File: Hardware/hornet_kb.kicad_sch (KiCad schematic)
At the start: 28 parts, among them J1 Conn_ST_STDC14, J10 USB_C_Receptacle_USB2.0, SW98 SW_Push, U1 nRF52840, Y1 32.768kHz, Y2 32MHz

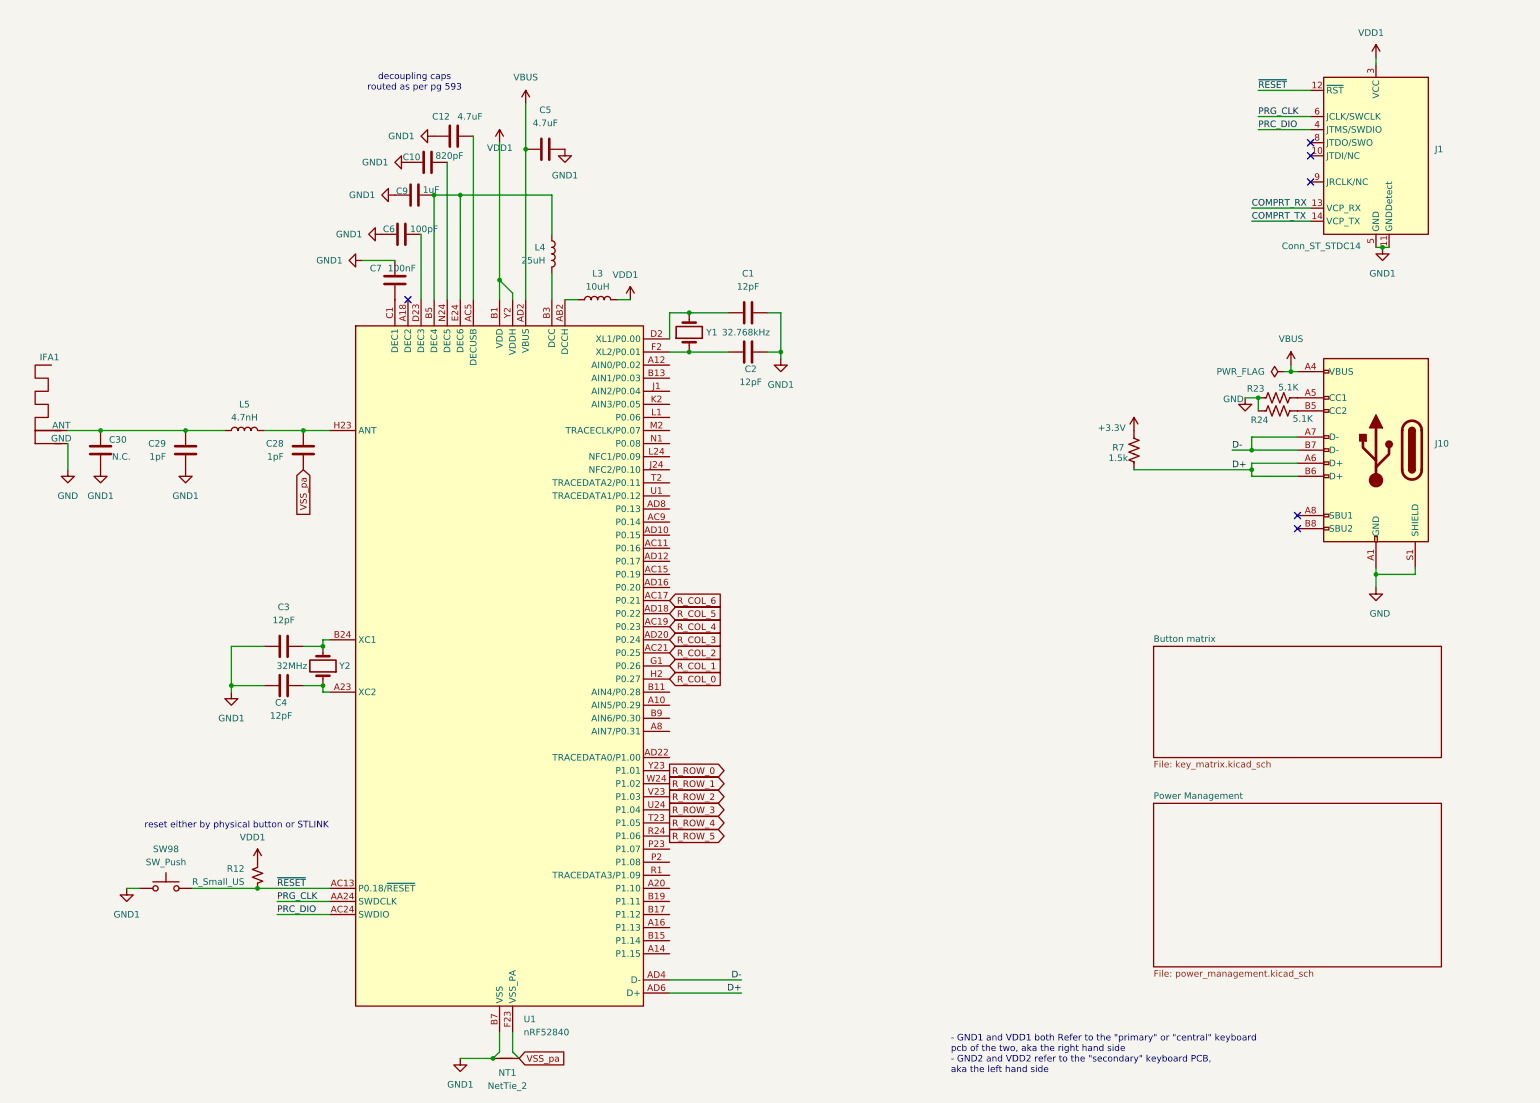
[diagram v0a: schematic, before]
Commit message: add datasheet to usb charger and fix erc
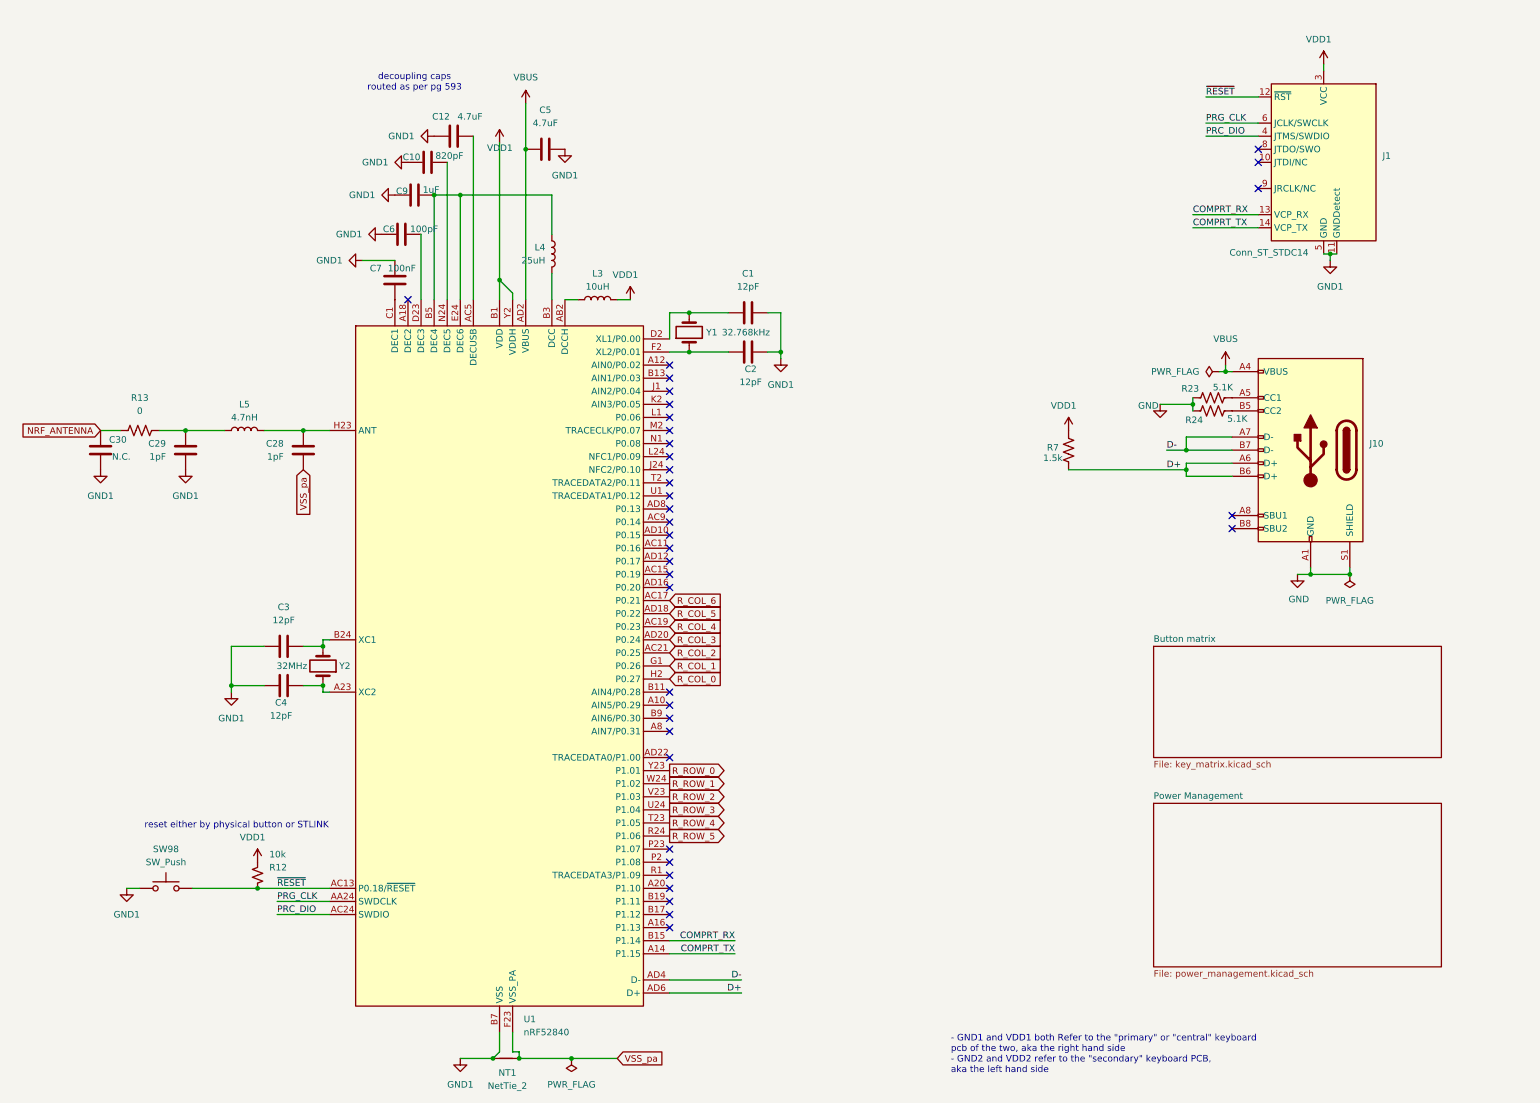
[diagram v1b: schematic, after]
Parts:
- removed IFA1: ~, symbol Device:IFA
- added R13: 0, symbol Device:R_US
- R12: value R_Small_US -> 10k
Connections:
- net +3.3V is gone; now on net VDD1: R7.1
- net COMPRT_RX: now also U1.B15 (P1.14)
- net COMPRT_TX: now also U1.A14 (P1.15)
- net at C29.1, L5.2: now also R13.2; no longer C30.1
- new net NRF_ANTENNA: C30.1, R13.1
- no-connect marks 6 -> 36
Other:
- moved on the sheet: J1, J10, R23, R24, R7

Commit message: Update footprints and switch symbol in schematic
Set proper SMD footprints for capacitors, resistors, inductors, crystals, and net ties in hornet_kb.kicad_sch. In power_management.kicad_sch, replace DIP switch symbol with DPDT switch, update related symbol properties, add new switch instance, and adjust wiring and annotation for improved clarity and functionality. Man i love summarize with copilot
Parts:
- C10, C6, C7, C9: footprint (none) -> Capacitor_SMD:C_0603_1608Metric
- C12, C5: footprint (none) -> Capacitor_SMD:C_0805_2012Metric
- C28, C29: footprint (none) -> Capacitor_SMD:C_0402_1005Metric
- L5: footprint (none) -> Inductor_SMD:L_0402_1005Metric
- NT1: footprint (none) -> NetTie:NetTie-2_SMD_Pad2.0mm
- R12: footprint (none) -> Resistor_SMD:R_0603_1608Metric
- R13: footprint (none) -> Resistor_SMD:R_0402_1005Metric
- Y1, Y2: footprint (none) -> Crystal:Crystal_SMD_3215-2Pin_3.2x1.5mm
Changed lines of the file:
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@@
 			)
 		)
-		(property "Footprint" ""
+		(property "Footprint" "Capacitor_SMD:C_0402_1005Metric"
 			(at 73.9648 102.87 0)
 			(effects
@@
 			)
 		)
-		(property "Footprint" ""
+		(property "Footprint" "Resistor_SMD:R_0603_1608Metric"
 			(at 66.04 181.61 0)
 			(effects
@@
 			)
 		)
-		(property "Footprint" ""
+		(property "Footprint" "Capacitor_SMD:C_0603_1608Metric"
 			(at 93.6752 62.23 0)
 			(effects
@@
 			)
 		)
-		(property "Footprint" ""
+		(property "Footprint" "Resistor_SMD:R_0402_1005Metric"
 			(at 43.434 94.234 90)
 			(effects
@@
 			)
 		)
-		(property "Footprint" ""
+		(property "Footprint" "NetTie:NetTie-2_SMD_Pad2.0mm"
 			(at 114.3 217.17 0)
 			(effects
@@
 			)
 		)
-		(property "Footprint" ""
+		(property "Footprint" "Inductor_SMD:L_0402_1005Metric"
 			(at 63.5 95.25 0)
 			(effects
@@
 			)
 		)
-		(property "Footprint" ""
+		(property "Footprint" "Capacitor_SMD:C_0603_1608Metric"
 			(at 90.17 56.1848 0)
 			(effects
@@
 			)
 		)
-		(property "Footprint" ""
+		(property "Footprint" "Crystal:Crystal_SMD_3215-2Pin_3.2x1.5mm"
 			(at 149.86 76.2 0)
 			(effects
@@
 			)
 		)
-		(property "Footprint" ""
+		(property "Footprint" "Capacitor_SMD:C_0805_2012Metric"
 			(at 118.11 39.6748 0)
 			(effects
@@
 			)
 		)
-		(property "Footprint" ""
+		(property "Footprint" "Capacitor_SMD:C_0805_2012Metric"
 			(at 100.33 37.1348 0)
 			(effects
@@
 			)
 		)
-		(property "Footprint" ""
+		(property "Footprint" "Capacitor_SMD:C_0603_1608Metric"
 			(at 92.71 48.5648 0)
 			(effects
@@
 			)
 		)
-		(property "Footprint" ""
+		(property "Footprint" "Crystal:Crystal_SMD_3215-2Pin_3.2x1.5mm"
 			(at 78.74 140.97 0)
 			(effects
@@
 			)
 		)
-		(property "Footprint" ""
+		(property "Footprint" "Capacitor_SMD:C_0402_1005Metric"
 			(at 51.1048 102.87 0)
 			(effects
@@
 			)
 		)
-		(property "Footprint" ""
+		(property "Footprint" "Capacitor_SMD:C_0603_1608Metric"
 			(at 102.87 44.1452 0)
 			(effects

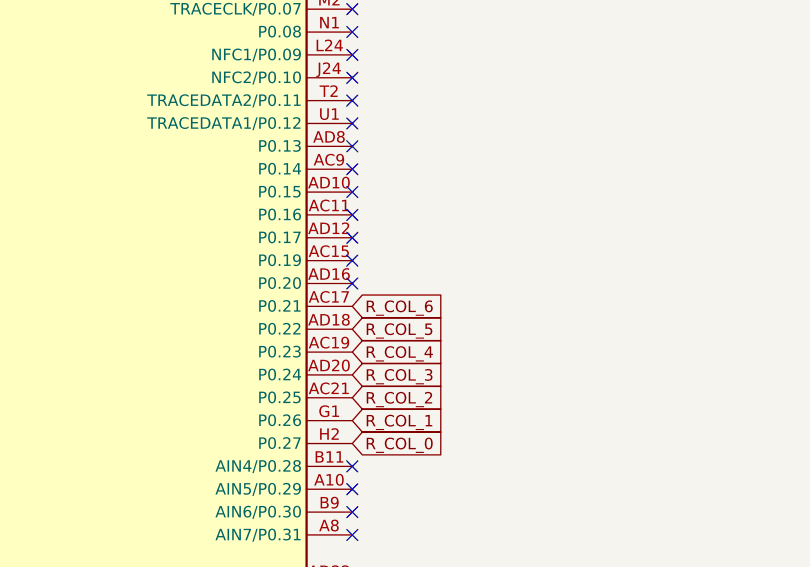
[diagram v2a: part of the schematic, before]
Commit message: Completed keymatrix layout
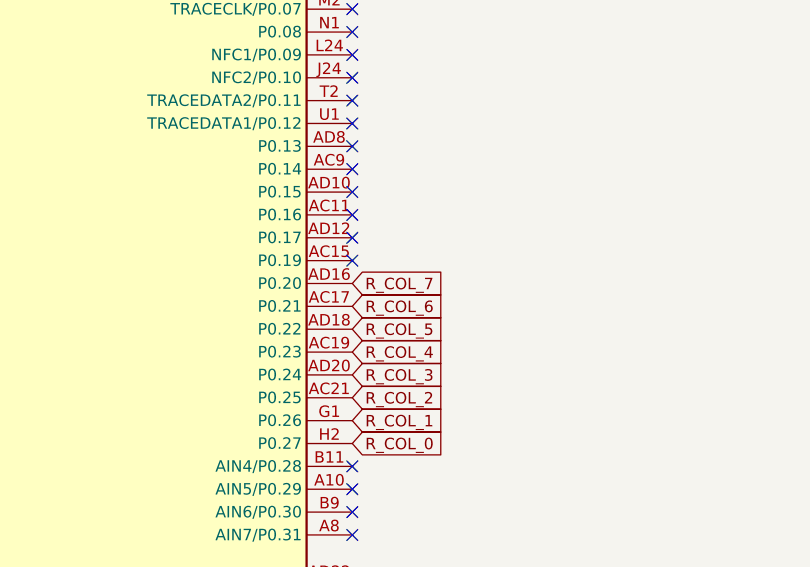
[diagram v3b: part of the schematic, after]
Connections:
- net R_COL_7: now reaches U1.AD16 (P0.20)
- no-connect marks 36 -> 35
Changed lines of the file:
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@@
 	)
 	(no_connect
-		(at 146.05 125.73)
-	)
-	(no_connect
 		(at 146.05 123.19)
 	)
@@
 			(effects
 				(font
+					(size 1.27 1.27)
+				)
+				(justify left)
+				(hide yes)
+			)
+		)
+	)
+	(global_label "R_COL_7"
+		(shape input)
+		(at 146.05 125.73 0)
+		(fields_autoplaced yes)
+		(effects
+			(font
+				(size 1.27 1.27)
+			)
+			(justify left)
+		)
+		(property "Intersheetrefs" "${INTERSHEET_REFS}"
+			(at 157.0785 125.73 0)
+			(effects
+				(font

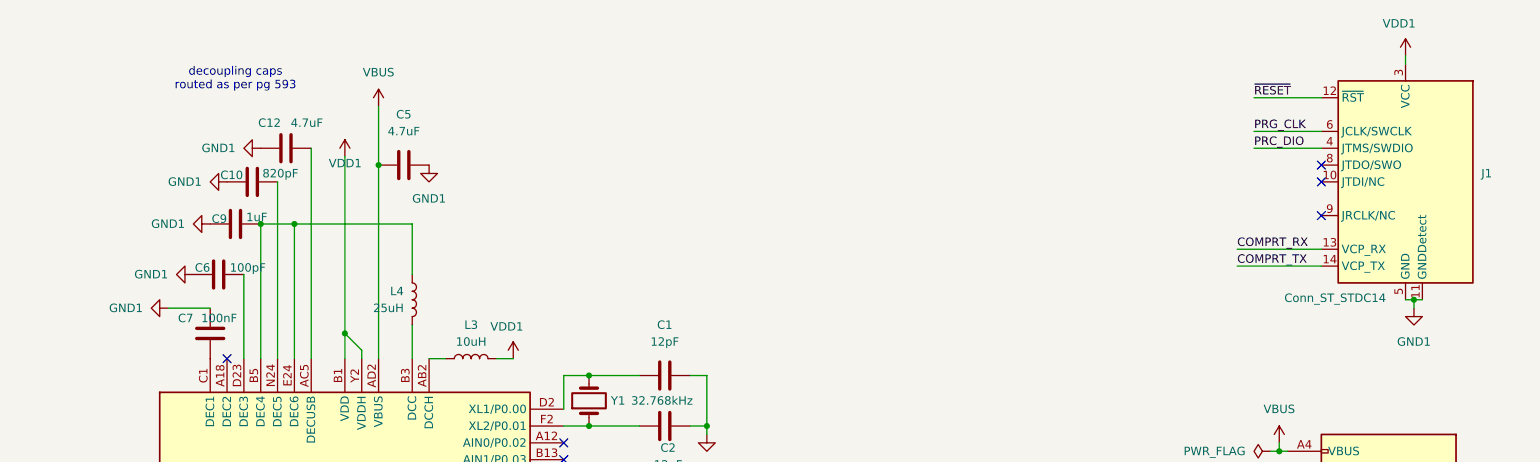
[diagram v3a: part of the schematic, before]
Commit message: Added LDO to battery and added placement for the charging modules
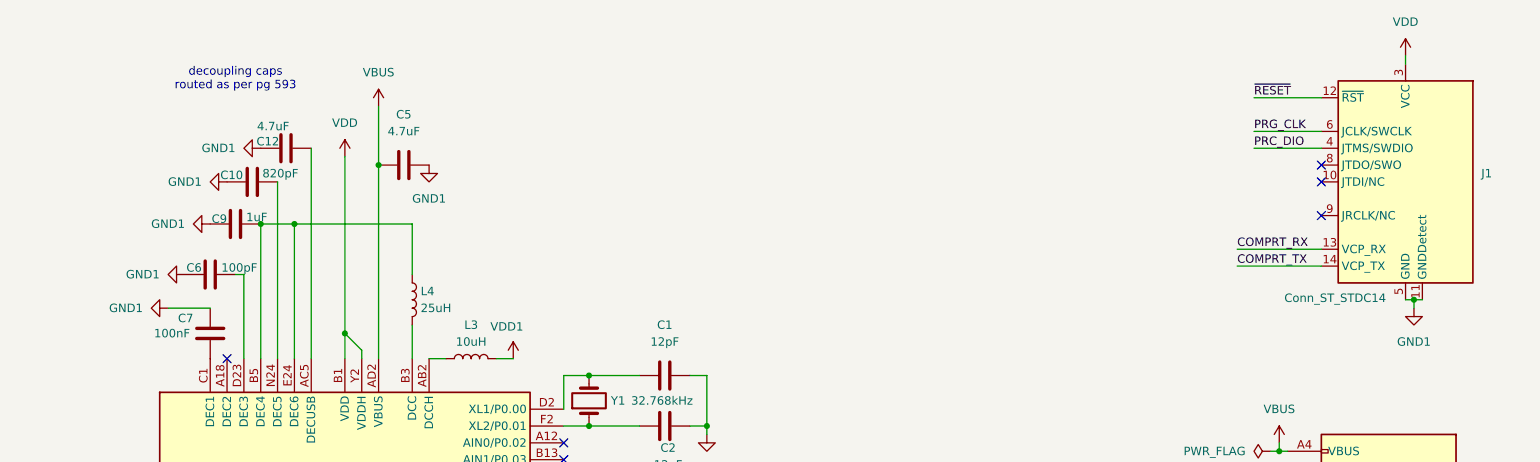
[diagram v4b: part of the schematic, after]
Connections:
- net VDD1: no longer J1.3 (VCC), U1.A22 (VDD), U1.AD14 (VDD), U1.AD23 (VDD), U1.B1 (VDD), U1.W1 (VDD), U1.Y2 (VDDH)
- new net VDD: J1.3 (VCC), U1.A22 (VDD), U1.AD14 (VDD), U1.AD23 (VDD), U1.B1 (VDD), U1.W1 (VDD), U1.Y2 (VDDH)
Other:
- moved on the sheet: C6
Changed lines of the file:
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@@
 	(wire
 		(pts
-			(xy 97.79 57.15) (xy 97.79 69.85)
-		)
-		(stroke
-			(width 0)
-			(type default)
-		)
-	)
-	(wire
-		(pts
 			(xy 158.75 194.31) (xy 146.05 194.31)
 		)
@@
 	(wire
 		(pts
+			(xy 96.52 57.15) (xy 97.79 57.15)
+		)
+		(stroke
+			(width 0)
+			(type default)
+		)
+	)
+	(wire
+		(pts
 			(xy 123.19 49.53) (xy 123.19 57.15)
 		)
@@
 	(wire
 		(pts
+			(xy 97.79 57.15) (xy 97.79 69.85)
+		)
+		(stroke
+			(width 0)
+			(type default)
+		)
+	)
+	(wire
+		(pts
 			(xy 274.32 62.23) (xy 274.32 60.96)
 		)
@@
 	)
 	(symbol
+		(lib_id "power:VDD")
+		(at 113.03 39.37 0)
+		(unit 1)
+		(exclude_from_sim no)
+		(in_bom yes)
+		(on_board yes)
+		(dnp no)
+		(fields_autoplaced yes)
+		(property "Reference" "#PWR08"
+			(at 113.03 43.18 0)
+			(effects
+				(font
+					(size 1.27 1.27)
+				)
+				(hide yes)
+			)
+		)
+		(property "Value" "VDD"
+			(at 113.03 34.29 0)
+			(effects
+				(font
+					(size 1.27 1.27)
+				)
+			)
+		)
+		(property "Footprint" ""
+			(at 113.03 39.37 0)
+			(effects
+				(font
+					(size 1.27 1.27)
+				)
+				(hide yes)
+			)
+		)
+		(property "Datasheet" ""
+			(at 113.03 39.37 0)
+			(effects
+				(font
+					(size 1.27 1.27)
+				)
+				(hide yes)
+			)
+		)
+		(property "Description" "Power symbol creates a global label with name \"VDD\""
+			(at 113.03 39.37 0)
+			(effects
+				(font
+					(size 1.27 1.27)
+				)
+				(hide yes)
+			)
+		)
+		(pin "1"
+		)
+		(instances
+			(project ""
+				(path "/c35084ab-104c-4a4c-9388-a839989b8e3d"
+					(reference "#PWR08")
+					(unit 1)
+				)
+			)
+		)
+	)
+	(symbol
 		(lib_id "Device:C")
 		(at 74.93 99.06 0)
@@
 		)
 		(property "Value" "100nF"
-			(at 96.774 63.754 0)
+			(at 89.662 66.04 0)
 			(effects
 				(font
@@
 	(symbol
 		(lib_id "power:GND1")
-		(at 90.17 57.15 270)
+		(at 88.9 57.15 270)
 		(mirror x)
 		(unit 1)
@@
 		(fields_autoplaced yes)
 		(property "Reference" "#PWR030"
-			(at 83.82 57.15 0)
+			(at 82.55 57.15 0)
 			(effects
 				(font
@@
 		)
 		(property "Value" "GND1"
-			(at 86.36 57.1499 90)
+			(at 85.09 57.1499 90)
 			(effects
 				(font
@@
 		)
 		(property "Footprint" ""
-			(at 90.17 57.15 0)
+			(at 88.9 57.15 0)
 			(effects
 				(font
@@
 		)
 		(property "Datasheet" ""
-			(at 90.17 57.15 0)
+			(at 88.9 57.15 0)
 			(effects
 				(font
@@
 		)
 		(property "Description" "Power symbol creates a global label with name \"GND1\" , ground"
-			(at 90.17 57.15 0)
+			(at 88.9 57.15 0)
 			(effects
 				(font
@@
 	)
 	(symbol
-		(lib_id "power:VDD")
-		(at 113.03 39.37 0)
-		(mirror y)
-		(unit 1)
-		(exclude_from_sim no)
-		(in_bom yes)
-		(on_board yes)
-		(dnp no)
-		(property "Reference" "#PWR08"
-			(at 113.03 43.18 0)
-			(effects
-				(font
-					(size 1.27 1.27)
-				)
-				(hide yes)
-			)
-		)
-		(property "Value" "VDD1"
-			(at 115.57 40.386 0)
-			(effects
-				(font
-					(size 1.27 1.27)
-				)
-				(justify left)
-			)
-		)
-		(property "Footprint" ""
-			(at 113.03 39.37 0)
-			(effects
-				(font
-					(size 1.27 1.27)
-				)
-				(hide yes)
-			)
-		)
-		(property "Datasheet" ""
-			(at 113.03 39.37 0)
-			(effects
-				(font
-					(size 1.27 1.27)
-				)
-				(hide yes)
-			)
-		)
-		(property "Description" "Power symbol creates a global label with name \"VDD\""
-			(at 113.03 39.37 0)
-			(effects
-				(font
-					(size 1.27 1.27)
-				)
-				(hide yes)
-			)
-		)
-		(pin "1"
-		)
-		(instances
-			(project ""
-				(path "/c35084ab-104c-4a4c-9388-a839989b8e3d"
-					(reference "#PWR08")
-					(unit 1)
-				)
-			)
-		)
-	)
-	(symbol
 		(lib_id "power:GND1")
 		(at 125.73 40.64 0)
@@
 	(symbol
 		(lib_id "Device:C")
-		(at 93.98 57.15 270)
+		(at 92.71 57.15 270)
 		(mirror x)
 		(unit 1)
@@
 		(dnp no)
 		(property "Reference" "C6"
-			(at 92.71 56.134 90)
+			(at 91.44 56.134 90)
 			(effects
 				(font
@@
 		)
 		(property "Value" "100pF"
-			(at 101.092 56.134 90)
+			(at 99.822 56.134 90)
 			(effects
 				(font
@@
 		)
 		(property "Footprint" "Capacitor_SMD:C_0603_1608Metric"
-			(at 90.17 56.1848 0)
+			(at 88.9 56.1848 0)
 			(effects
 				(font
@@
 		)
 		(property "Datasheet" "~"
-			(at 93.98 57.15 0)
+			(at 92.71 57.15 0)
 			(effects
 				(font
@@
 		)
 		(property "Description" "Unpolarized capacitor"
-			(at 93.98 57.15 0)
+			(at 92.71 57.15 0)
 			(effects
 				(font
@@
 		(on_board yes)
 		(dnp no)
-		(fields_autoplaced yes)
 		(property "Reference" "L4"
-			(at 121.92 59.6899 0)
+			(at 124.46 59.69 0)
 			(effects
 				(font
 					(size 1.27 1.27)
 				)
-				(justify right)
+				(justify left)
 			)
 		)
 		(property "Value" "25uH"
-			(at 121.92 62.2299 0)
+			(at 124.46 62.23 0)
 			(effects
 				(font
 					(size 1.27 1.27)
 				)
-				(justify right)
+				(justify left)
 			)
 		)
@@
 		(dnp no)
 		(property "Reference" "C12"
-			(at 103.378 34.29 90)
+			(at 103.124 37.084 90)
 			(effects
 				(font
@@
 		)
 		(property "Value" "4.7uF"
-			(at 109.728 34.29 90)
+			(at 104.648 34.798 90)
 			(effects
 				(font
@@
 		(lib_id "power:VDD")
 		(at 273.05 24.13 0)
-		(mirror y)
 		(unit 1)
 		(exclude_from_sim no)
@@
 		(on_board yes)
 		(dnp no)
-		(property "Reference" "#PWR041"
+		(fields_autoplaced yes)
+		(property "Reference" "#PWR015"
 			(at 273.05 27.94 0)
 			(effects
@@
 			)
 		)
-		(property "Value" "VDD1"
-			(at 274.574 19.304 0)
+		(property "Value" "VDD"
+			(at 273.05 19.05 0)
 			(effects
 				(font
 					(size 1.27 1.27)
 				)
-				(justify left)
 			)
 		)
@@
 			(project "hornet_kb"
 				(path "/c35084ab-104c-4a4c-9388-a839989b8e3d"
-					(reference "#PWR041")
+					(reference "#PWR015")
 					(unit 1)
 				)
